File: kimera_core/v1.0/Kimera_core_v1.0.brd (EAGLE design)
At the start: 26 x 12 mm, 21 parts, among them IC1 PCA9555RGER-NOPAD, IC2 PCA9555RGER-NOPAD, Q1 CSTCR6M00G53Z, U1 ATMEGA32U4QFN2

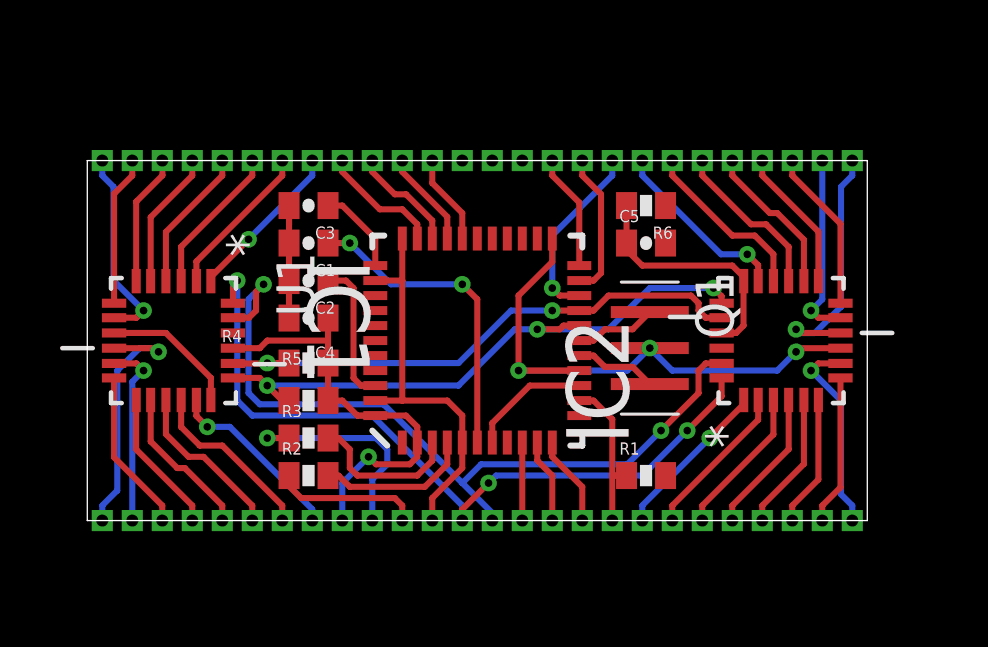
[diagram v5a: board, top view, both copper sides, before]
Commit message: kimera_core: First complete version - Finish routing - Add logo and silk screen
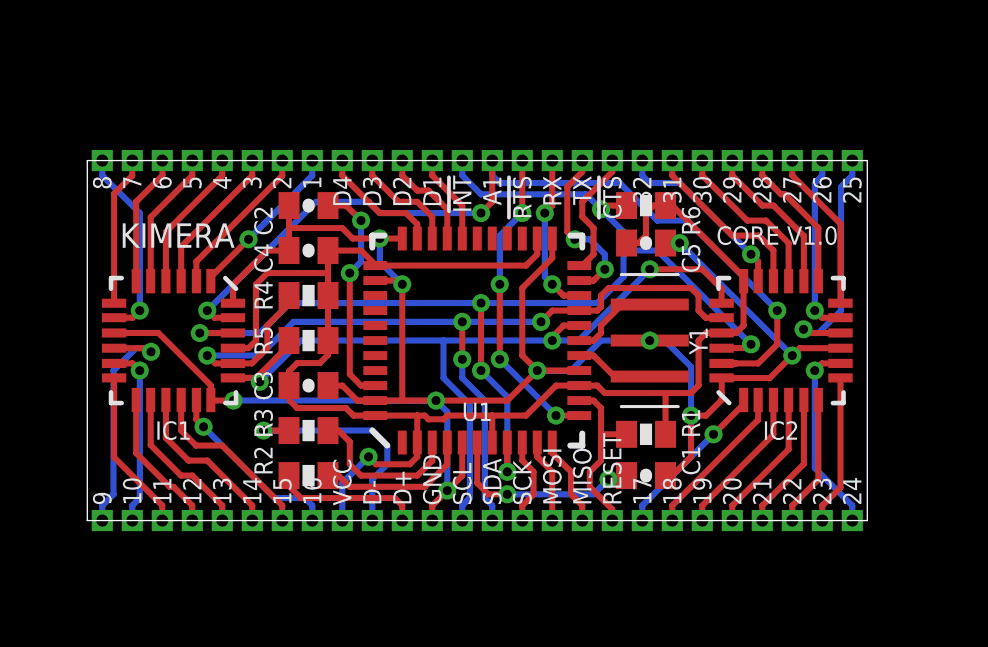
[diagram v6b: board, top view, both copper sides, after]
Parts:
- removed Q1: CSTCR6M00G53Z, cstce-resonator:CSTER12M
- added LOGO1: KIMERA_LOGO, logo:KIMERA_LOGO
- added LOGO2: NOUKENSHA_LOGONIX, logo:NOUKENSHA_LOGO_NIX
- added LOGO3: OSHW_LOGONIX, logo:OSHW_LOGO_NIX
- added Y1: CSTCR6M00G53Z, cstce-resonator:CSTER12M
- moved C1 13.7 mm to (18.6, 1.50), turned to 0 degrees
- moved C3 6.00 mm to (7.38, 4.50), turned to 0 degrees
- moved C2 2.50 mm to (7.38, 10.5)
- moved C4 2.25 mm to (7.38, 9.00)
- moved R4 2.25 mm to (7.38, 7.50)
- moved R5 2.00 mm to (7.38, 6.00)
- moved R1 1.38 mm to (18.6, 2.88)
- moved R3 0.25 mm to (7.38, 3.00)
- turned R6 to 0 degrees
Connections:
- net /RTS renamed !RTS
- removed net /CTS: JP6.3, U1.22
- removed net A2: IC1.24, IC2.24, JP5.5
- removed net N$12: IC1.22, IC2.22, R6.1
- new net !CTS: JP6.1, U1.22
- new net !INT: IC1.22, IC2.22, JP6.6, R6.1, U1.8
- net A1: now also JP6.5; no longer JP5.6
- net GND: now also IC1.24, IC2.24, Y1.2; no longer Q1.2
- net N$3: now also Y1.1; no longer Q1.1
- net N$4: now also Y1.3; no longer Q1.3
- net RX: now also JP6.3; no longer JP6.1
- net SCL: now also JP5.5; no longer JP6.5
- net SDA: now also JP5.6; no longer JP6.6
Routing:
- net !INT: track 0.00 -> 38.6 mm, vias 0 -> 6
- net GND: track 40.9 -> 69.4 mm, vias 3 -> 10
- net A2: track 25.5 -> 0.00 mm, vias 3 -> 0
- net VCC: track 29.9 -> 52.4 mm
- net SDA: track 18.4 -> 30.4 mm, vias 2 -> 4
- net !RTS: track 0.27 -> 10.4 mm, vias 0 -> 4
- net SCL: track 20.5 -> 28.0 mm
- net !CTS: track 0.00 -> 4.32 mm
- net /CTS: track 3.87 -> 0.00 mm
- net N$6: track 10.5 -> 6.74 mm
- net N$1: track 4.78 -> 7.59 mm, vias 0 -> 2
- net A1: track 26.4 -> 29.2 mm, vias 2 -> 3
- net TX: track 4.84 -> 5.65 mm, vias 0 -> 2
- net RX: track 6.08 -> 5.39 mm, vias 1 -> 2
- net RESET: track 5.21 -> 5.89 mm
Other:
- board text added: "!CTS"
- board text added: "!INT"
- board text added: "!RTS"
- board text added: "1"
- board text added: "10"
- board text added: "11"
- board text added: "12"
- board text added: "13"
- board text added: "14"
- board text added: "15"
- board text added: "16"
- board text added: "17"
- board text added: "18"
- board text added: "19"
- board text added: "2"
- board text added: "20"
- board text added: "21"
- board text added: "22"
- board text added: "23"
- board text added: "24"
- board text added: "25"
- board text added: "26"
- board text added: "27"
- board text added: "28"
- board text added: "29"
- board text added: "3"
- board text added: "30"
- board text added: "31"
- board text added: "32"
- board text added: "4"
- board text added: "5"
- board text added: "6"
- board text added: "7"
- board text added: "8"
- board text added: "9"
- board text added: "A1"
- board text added: "CORE V1.0"
- board text added: "D+"
- board text added: "D-"
- board text added: "D1"
- board text added: "D2"
- board text added: "D3"
- board text added: "D4"
- board text added: "GND"
- board text added: "KIMERA"
- board text added: "MISO"
- board text added: "MOSI"
- board text added: "RESET"
- board text added: "RX"
- board text added: "SCK"
- board text added: "SCL"
- board text added: "SDA"
- board text added: "TX"
- board text added: "VCC"
